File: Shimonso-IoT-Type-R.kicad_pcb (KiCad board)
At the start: 4 copper layers, 85 x 54 mm, 116 parts, among them CON1 96Boards_HS_connector, CON2 96Boards_LS_connector, CON3 microUSB_CONSOLE, CON4 CONN_01X15, CON5 CONN_01X15, Q1 S8050, SW1 RST, U1 FT230X, U10 PCA9306DC1, U11 bm1422gmv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

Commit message: DRC_ok
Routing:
- net /BM1422GMV_DRDY: track 0.00 -> 77.6 mm, vias 0 -> 4
- net /1V8: track 220.8 -> 279.6 mm, vias 16 -> 22
- net /KX022-1020_INT1: track 0.00 -> 37.2 mm, vias 0 -> 2
- net GND: track 338.5 -> 351.0 mm, vias 61 -> 65
- net Net-(U15-Pad4): track 0.00 -> 5.92 mm
- net /ISP1_SDA: track 47.3 -> 52.1 mm, vias 2 -> 3
- net Net-(CB21-Pad1): track 0.00 -> 3.63 mm, vias 0 -> 1
- net /PMU_PWRON_N: track 56.9 -> 59.7 mm
- net /3V3: track 116.3 -> 118.8 mm, vias 26 -> 27
- net /EXP_RSTOUT_N: track 60.9 -> 61.6 mm
- net Net-(CB13-Pad1): track 8.53 -> 9.03 mm
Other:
- net class 0.2: clearance 0.2 -> 0.15
- net class Default: clearance 0.25 -> 0.2
- rule trace_clearance: 0.25 -> 0.2

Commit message: modified
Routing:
- net GND: track 351.0 -> 349.1 mm, vias 65 -> 67
- net Net-(PAD1-Pad1): track 6.90 -> 8.53 mm
- net /3V3: track 118.8 -> 119.3 mm
- net Net-(CB12-Pad1): track 7.25 -> 7.75 mm
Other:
- rule pad_to_mask_clearance: 0 -> 0.1

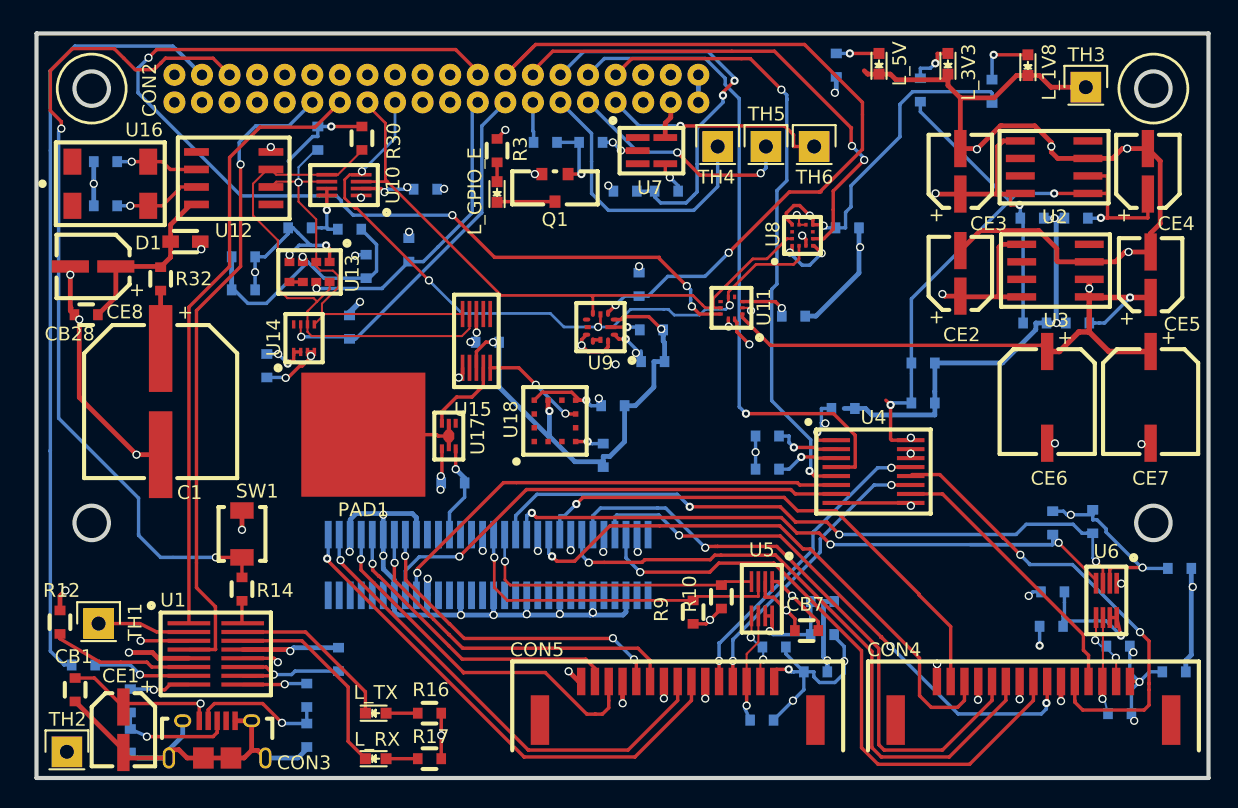
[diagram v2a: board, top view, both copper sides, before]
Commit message: change to autorout pcb
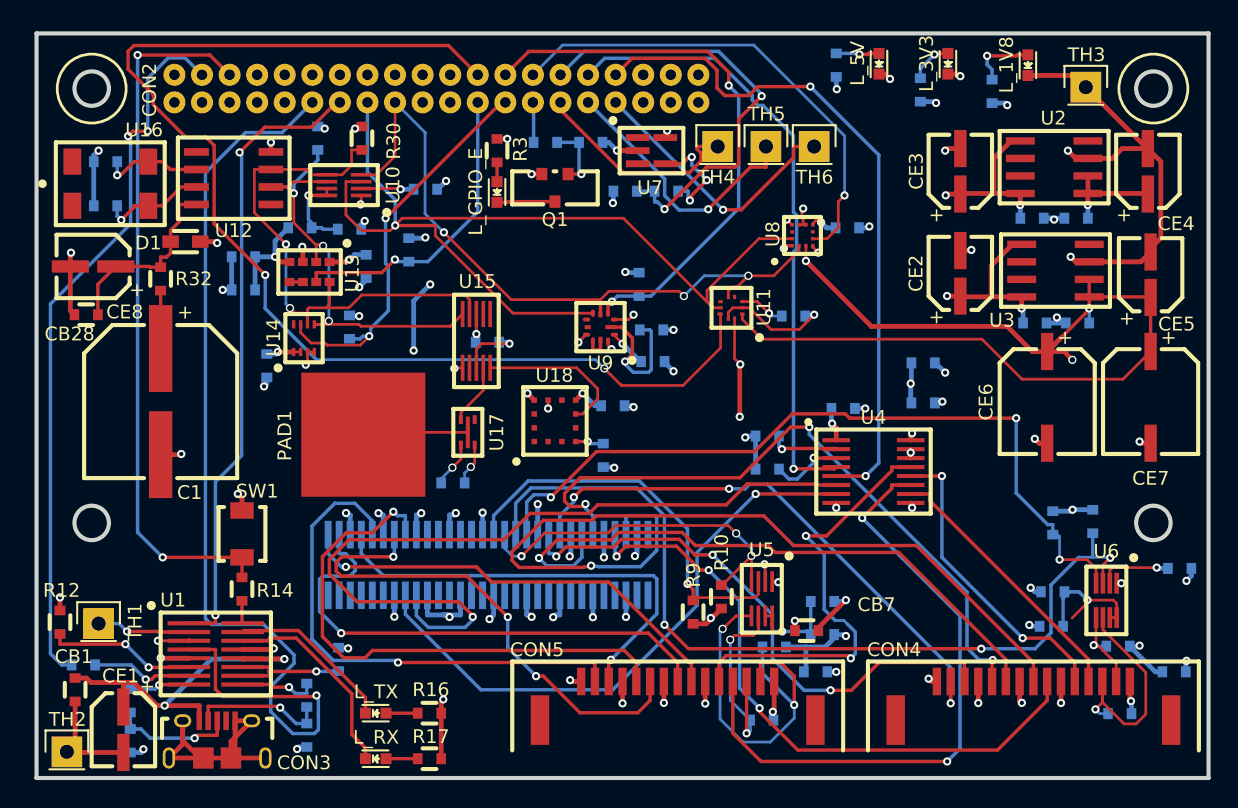
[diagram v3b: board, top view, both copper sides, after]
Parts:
- U17: footprint rohm:BD1020HFV -> rohm:BD1020HFV_test
- moved U17 1.41 mm to (81.3, 124.9)
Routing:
- net GND: track 349.1 -> 691.1 mm, vias 67 -> 84
- net /3V3: track 119.3 -> 252.6 mm, vias 27 -> 21
- net /UART3_TX: track 47.2 -> 73.7 mm
- net /CAM1_CLK_3V3: track 21.1 -> 45.8 mm
- net /I2C0_SCL: track 46.3 -> 70.0 mm, vias 0 -> 1
- net /CAM1_CLK: track 35.0 -> 58.2 mm
- net /ISP0_SDA_3V3: track 5.32 -> 28.3 mm
- net /BM1383GLV_INT: track 58.4 -> 40.7 mm
- net /CSI1_CLK_N: track 45.5 -> 62.5 mm
- net /CSI0_DATA1_N: track 24.0 -> 40.0 mm, vias 3 -> 1
- net /CSI0_DATA0_N: track 22.6 -> 37.4 mm
- net /ISP1_SCL: track 49.6 -> 63.9 mm
- net /CAM2_GPIO_3V3: track 34.3 -> 22.3 mm
- net /BM1422GMV_DRDY: track 77.6 -> 89.2 mm, vias 4 -> 2
- net /CSI0_DATA1_P: track 26.0 -> 36.7 mm, vias 1 -> 3
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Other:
- net class 0.15 removed
- net class 0.2 removed
- net class 1V8: clearance 0.4 -> 0.2; trace_width 0.4 -> 0.2
- net class 3V3 added: clearance 0.2, trace_width 0.2, via_dia 0.6, via_drill 0.4
- net class 3V5 removed
- net class 5V: trace_width 0.25 -> 0.35
- net class Default: trace_width 0.25 -> 0.2
- net class GND: clearance 0.25 -> 0.2; trace_width 0.35 -> 0.2
- net class I2C added: clearance 0.2, trace_width 0.2, via_dia 0.6, via_drill 0.4
- net class SCL_SDA removed
- net class SCL_SDA_3V3 removed
